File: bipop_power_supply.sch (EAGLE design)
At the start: 32 parts, among them IC1 LM1117MP-3.3, IC2 LM1117MP-5.0, X2 MSTBA6

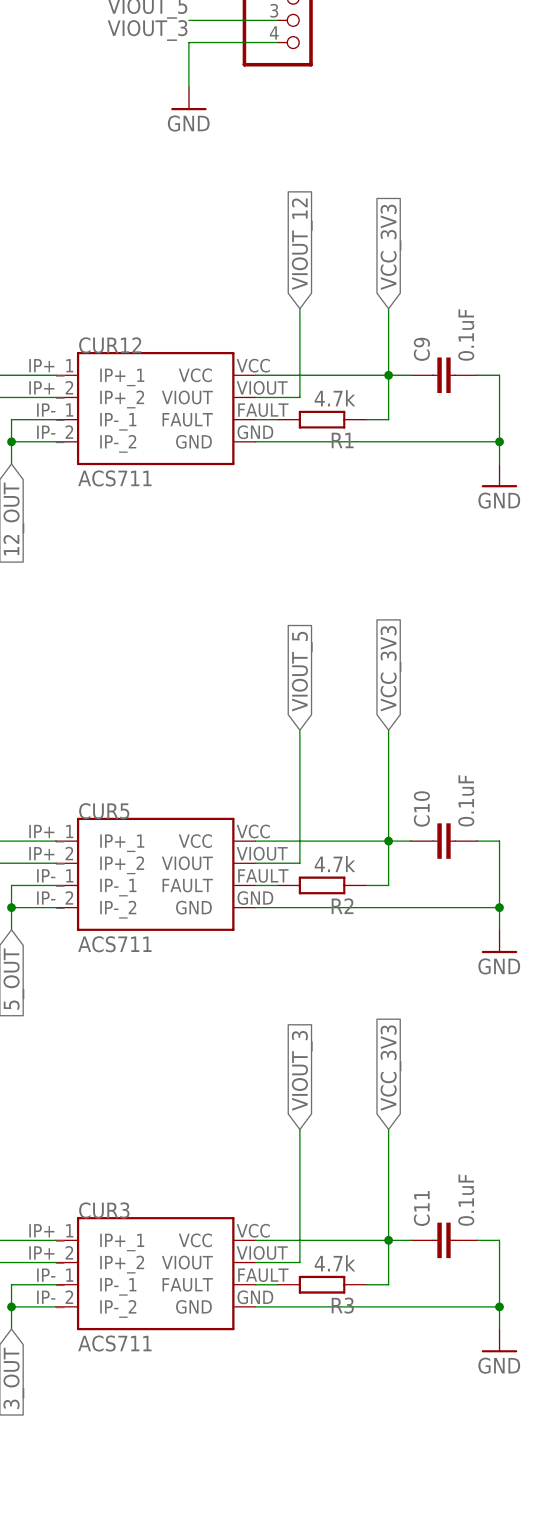
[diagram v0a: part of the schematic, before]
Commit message: PS poprawione, dodane pullupy
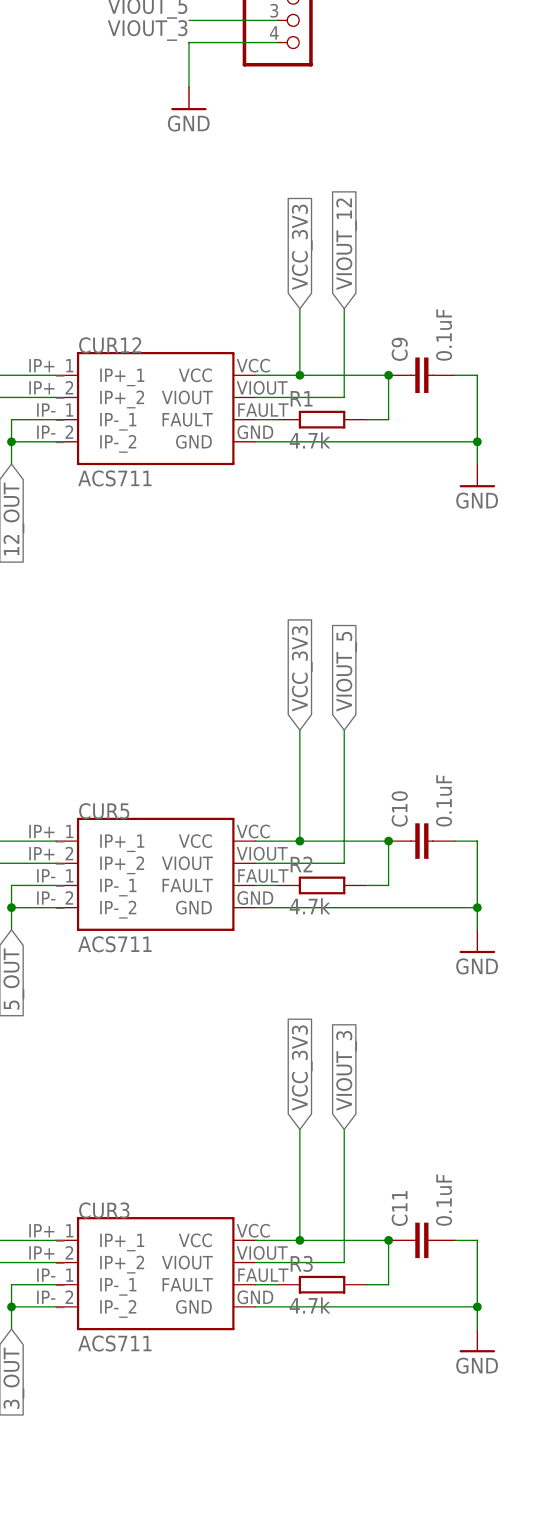
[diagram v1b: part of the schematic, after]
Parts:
- R1, R2, R3: device resistor:R-EU_R0805 -> rcl:R-EU_R0805
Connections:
- net N$1: now also CUR3.FAULT, R3.1; no longer CUR12.FAULT, R1.2
- net N$4: now also R2.1; no longer R2.2
- net N$7: now also CUR12.FAULT, R1.1; no longer CUR3.FAULT, R3.2
- net VCC_3V3: now also R1.2, R2.2, R3.2; no longer R1.1, R2.1, R3.1
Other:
- moved on the sheet: C10, C11, C9, R1, R2, R3

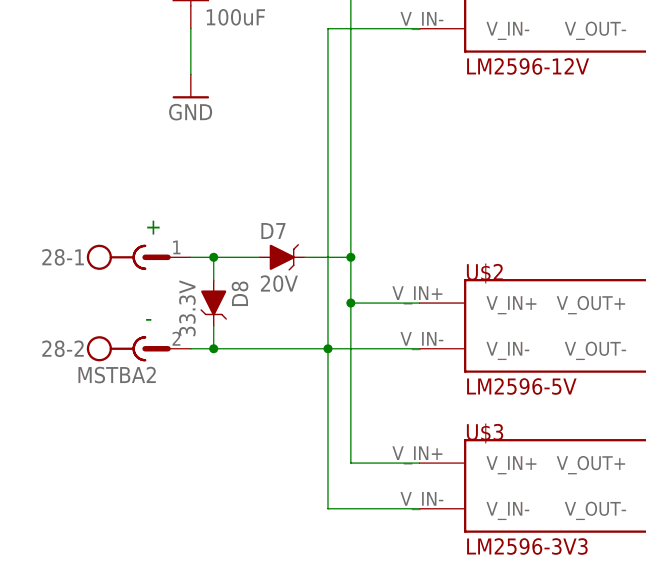
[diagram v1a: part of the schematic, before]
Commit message: changed diodes' packages
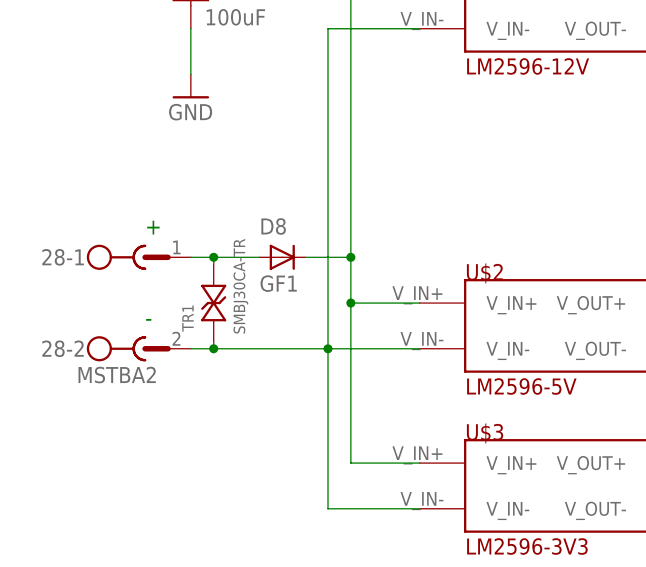
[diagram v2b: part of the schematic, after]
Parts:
- removed D7: 20V, SparkFun-DiscreteSemi:DIODE-ZENER-MM3Z3V3T1G
- added TR1: SMBJ30CA-TR, transil:SMAJ30CA-TR__DO214AC
- D8: value 33.3V -> GF1; device SparkFun-DiscreteSemi:DIODE-ZENER-MM3Z3V3T1G -> _mod_diode:GF1
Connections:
- net MM: now also D8.C; no longer D7.C
- net N$10: now also TR1.P$1; no longer D8.C
- net N$12: now also TR1.P$2; no longer D7.A
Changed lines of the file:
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@@
 <part name="IC2" library="lm1117_10" deviceset="LM1117?-*" device="MP" technology="5.0"/>
 <part name="FRAME1" library="frames" library_urn="urn:adsk.eagle:library:229" deviceset="DINA4_P" device=""/>
-<part name="D7" library="SparkFun-DiscreteSemi" deviceset="DIODE-ZENER" device="-MM3Z3V3T1G" value="20V"/>
 <part name="C1" library="rcl" library_urn="urn:adsk.eagle:library:334" deviceset="C-EU" device="C0805" package3d_urn="urn:adsk.eagle:package:23617/2" value="100uF"/>
-<part name="D8" library="SparkFun-DiscreteSemi" deviceset="DIODE-ZENER" device="-MM3Z3V3T1G" value="33.3V"/>
 <part name="C2" library="rcl" library_urn="urn:adsk.eagle:library:334" deviceset="C-EU" device="C0805" package3d_urn="urn:adsk.eagle:package:23617/2" value="100uF"/>
 <part name="C3" library="rcl" library_urn="urn:adsk.eagle:library:334" deviceset="C-EU" device="C0805" package3d_urn="urn:adsk.eagle:package:23617/2" value="100uF"/>
@@
 <part name="R2" library="rcl" library_urn="urn:adsk.eagle:library:334" deviceset="R-EU_" device="R0805" package3d_urn="urn:adsk.eagle:package:23553/2" value="4.7k"/>
 <part name="R3" library="rcl" library_urn="urn:adsk.eagle:library:334" deviceset="R-EU_" device="R0805" package3d_urn="urn:adsk.eagle:package:23553/2" value="4.7k"/>
+<part name="TR1" library="transil" deviceset="SMAJ30CA-TR__DO214AC" device="" value="SMBJ30CA-TR"/>
+<part name="D8" library="_mod_diode" deviceset="GF1" device=""/>
 </parts>
 <sheets>
@@
 <instance part="FRAME1" gate="G$1" x="-30.48" y="-101.6"/>
 <instance part="FRAME1" gate="G$2" x="48.26" y="-101.6"/>
-<instance part="D7" gate="G$1" x="-5.08" y="22.86"/>
 <instance part="C1" gate="G$1" x="-15.24" y="91.44"/>
-<instance part="D8" gate="G$1" x="-12.7" y="17.78" rot="R270"/>
 <instance part="C2" gate="G$1" x="-15.24" y="78.74"/>
 <instance part="C3" gate="G$1" x="-15.24" y="66.04"/>
@@
 <instance part="R2" gate="G$1" x="203.2" y="15.24"/>
 <instance part="R3" gate="G$1" x="203.2" y="-30.48"/>
+<instance part="TR1" gate="G$1" x="-12.7" y="17.78" rot="R90"/>
+<instance part="D8" gate="D" x="-5.08" y="22.86"/>
 </instances>
 <busses>
@@
 <net name="N$10" class="0">
 <segment>
-<pinref part="D8" gate="G$1" pin="C"/>
-<wire x1="-12.7" y1="12.7" x2="-15.24" y2="12.7" width="0.1524" layer="91"/>
-<wire x1="-12.7" y1="15.24" x2="-12.7" y2="12.7" width="0.1524" layer="91"/>
 <pinref part="U$1" gate="G$1" pin="V_IN-"/>
 <wire x1="0" y1="48.26" x2="0" y2="12.7" width="0.1524" layer="91"/>
 <wire x1="0" y1="12.7" x2="0" y2="-5.08" width="0.1524" layer="91"/>
 <pinref part="U$2" gate="G$1" pin="V_IN-"/>
-<wire x1="-12.7" y1="12.7" x2="0" y2="12.7" width="0.1524" layer="91"/>
-<junction x="-12.7" y="12.7"/>
+<wire x1="-15.24" y1="12.7" x2="-12.7" y2="12.7" width="0.1524" layer="91"/>
 <junction x="0" y="12.7"/>
 <pinref part="U$3" gate="G$1" pin="V_IN-"/>
+<wire x1="-12.7" y1="12.7" x2="0" y2="12.7" width="0.1524" layer="91"/>
 <wire x1="10.16" y1="-5.08" x2="0" y2="-5.08" width="0.1524" layer="91"/>
 <wire x1="10.16" y1="12.7" x2="0" y2="12.7" width="0.1524" layer="91"/>
 <wire x1="10.16" y1="48.26" x2="0" y2="48.26" width="0.1524" layer="91"/>
 <pinref part="28" gate="-2" pin="1"/>
+<pinref part="TR1" gate="G$1" pin="P$1"/>
+<wire x1="-12.7" y1="13.335" x2="-12.7" y2="12.7" width="0.1524" layer="91"/>
+<junction x="-12.7" y="12.7"/>
 </segment>
 </net>
 <net name="N$12" class="0">
 <segment>
-<wire x1="-15.24" y1="22.86" x2="-12.7" y2="22.86" width="0.1524" layer="91"/>
-<pinref part="D8" gate="G$1" pin="A"/>
-<wire x1="-12.7" y1="20.32" x2="-12.7" y2="22.86" width="0.1524" layer="91"/>
-<pinref part="D7" gate="G$1" pin="A"/>
 <wire x1="-7.62" y1="22.86" x2="-12.7" y2="22.86" width="0.1524" layer="91"/>
+<pinref part="28" gate="-1" pin="1"/>
+<pinref part="TR1" gate="G$1" pin="P$2"/>
+<wire x1="-12.7" y1="22.86" x2="-15.24" y2="22.86" width="0.1524" layer="91"/>
+<wire x1="-12.7" y1="22.225" x2="-12.7" y2="22.86" width="0.1524" layer="91"/>
 <junction x="-12.7" y="22.86"/>
-<pinref part="28" gate="-1" pin="1"/>
+<pinref part="D8" gate="D" pin="A"/>
 </segment>
 </net>
@@
 <pinref part="U$1" gate="G$1" pin="V_IN+"/>
 <wire x1="2.54" y1="17.78" x2="2.54" y2="0" width="0.1524" layer="91"/>
-<pinref part="D7" gate="G$1" pin="C"/>
 <wire x1="-2.54" y1="22.86" x2="2.54" y2="22.86" width="0.1524" layer="91"/>
 <junction x="2.54" y="22.86"/>
@@
 <junction x="2.54" y="17.78"/>
 <wire x1="10.16" y1="53.34" x2="2.54" y2="53.34" width="0.1524" layer="91"/>
-</segment>
-</net>
+<pinref part="D8" gate="D" pin="C"/>
+</segment>
+</net>
